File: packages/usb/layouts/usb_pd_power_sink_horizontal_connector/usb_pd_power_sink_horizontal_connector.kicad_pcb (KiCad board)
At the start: 2 copper layers, 8 parts, among them U2 2.9V

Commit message: WIP update usb
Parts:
- C1: value 1µF ±10% 16V X5R -> 1µF ±10% 25V X5R; footprint atopile:C0402-b3ef17 -> Samsung_Electro_Mechanics_CL05A105KA5NQNC:C0402
- R1, R2, R4: footprint atopile:R0402-56259e -> UNI_ROYAL_0402WGF1002TCE:R0402
- R3: footprint atopile:R0402-56259e -> UNI_ROYAL_0402WGF1001TCE:R0402
- U1: footprint atopile:ESSOP-10_L4.9-W3.9-P1.0-LS6.0-TL-EP-20a8ca -> WCH_CH224K:ESSOP-10_L4.9-W3.9-P1.0-LS6.0-TL-EP
- U2: footprint lib:LED0603-RD -> Hubei_KENTO_Elec_Blue_light_0603:LED0603-RD
- X1: footprint atopile:USB-C-SMD_TYPE-C-6PIN-2MD-073-1d78f0 -> SHOU_HAN_TYPE_C_16PIN_2MD_073:USB-C-SMD_TYPE-C-6PIN-2MD-073
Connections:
- U1 pad 2: pd_trigger.controller-line -> pd_trigger.controller-line-1
- U1 pad 3: pd_trigger.controller-line-1 -> pd_trigger.controller-line
- U1 pad 4: line-1 -> line-4
- U1 pad 6: line -> line-5
- X1 pad : (no net) -> net
- X1 pad 10: line -> line-5
- X1 pad 3: line-4 -> line
- X1 pad 6: line-1 -> line-4
- X1 pad 8: line-1 -> line-4
- X1 pad 9: line-5 -> line-1
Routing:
- net line-5: track 0.00 -> 13.6 mm, vias 0 -> 2
- net line: track 13.6 -> 0.00 mm, vias 2 -> 0
- net line-4: track 0.00 -> 8.15 mm, vias 0 -> 2
- net line-1: track 8.15 -> 0.00 mm, vias 2 -> 0

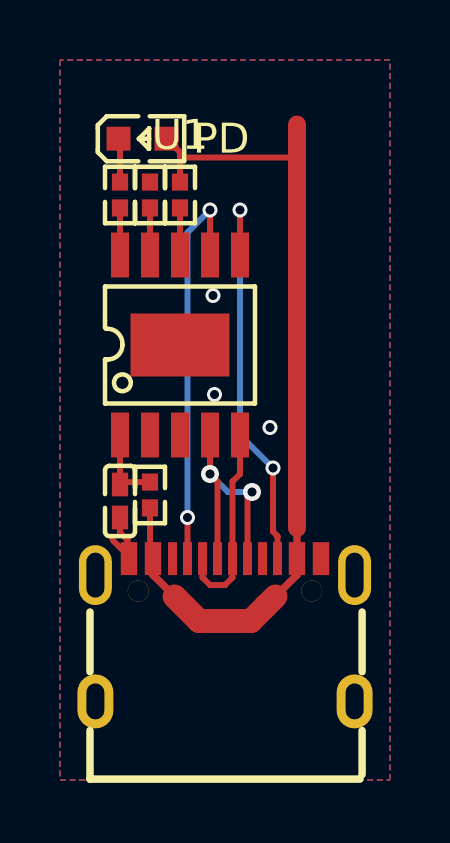
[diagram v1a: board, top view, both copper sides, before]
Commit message: Manually fix fp lib tables
fix some small bugs
fix package only modules (e.g. logos)
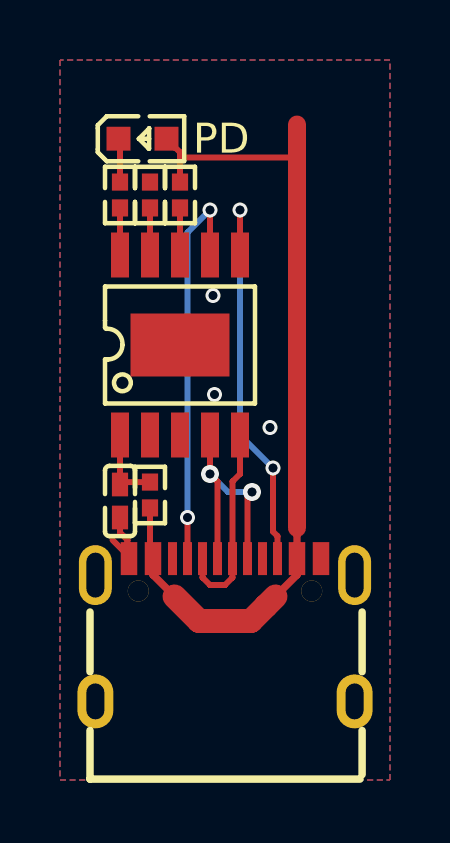
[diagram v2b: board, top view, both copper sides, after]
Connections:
- U1 pad 2: pd_trigger.controller-line-1 -> pd_trigger.controller-line
- U1 pad 3: pd_trigger.controller-line -> pd_trigger.controller-line-1
- U1 pad 4: line-4 -> line-1
- U1 pad 5: line-2 -> line-4
- U1 pad 6: line-5 -> line-2
- U1 pad 7: line-3 -> line
- X1 pad 10: line-5 -> line-2
- X1 pad 3: line -> line-3
- X1 pad 4: line-3 -> line
- X1 pad 5: line-2 -> line-4
- X1 pad 6: line-4 -> line-1
- X1 pad 7: line-2 -> line-4
- X1 pad 8: line-4 -> line-1
- X1 pad 9: line-1 -> line-5
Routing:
- net line-5: track 13.6 -> 0.00 mm, vias 2 -> 0
- net line-3: track 13.4 -> 0.00 mm, vias 2 -> 0
- net line: track 0.00 -> 13.4 mm, vias 0 -> 2
- net line-1: track 0.00 -> 8.15 mm, vias 0 -> 2
- net line-2: track 6.69 -> 13.6 mm, vias 0 -> 2
- net line-4: track 8.15 -> 6.69 mm, vias 2 -> 0

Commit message: rebuild all packages & regenerate images of changed layouts (silk)
Add new scripts for version bump and build (based on atopile/packages)
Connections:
- R2 pad 2: pd_trigger-line -> pd_trigger-line-1
- R4 pad 1: pd_trigger-line-1 -> pd_trigger-line
- U1 pad 4: line-1 -> line-5
- U1 pad 6: line-2 -> line-1
- U1 pad 8: pd_trigger-line -> pd_trigger-line-1
- U1 pad 9: pd_trigger-line-1 -> pd_trigger-line
- X1 pad 10: line-2 -> line-1
- X1 pad 6: line-1 -> line-5
- X1 pad 8: line-1 -> line-5
- X1 pad 9: line-5 -> line-2
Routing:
- net line-2: track 13.6 -> 0.00 mm, vias 2 -> 0
- net line-5: track 0.00 -> 8.15 mm, vias 0 -> 2
- net line-1: track 8.15 -> 13.6 mm
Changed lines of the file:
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@@
     (net 1 "pd_trigger.controller-line-1")
     (net 2 "pd_trigger.controller-line")
-    (net 3 "pd_trigger-line")
+    (net 3 "pd_trigger-line-1")
     (net 4 "hv")
-    (net 5 "pd_trigger-line-1")
+    (net 5 "pd_trigger-line")
     (net 6 "pd_trigger-gnd")
     (net 7 "cathode")
-    (net 8 "line-2")
+    (net 8 "line-1")
     (net 9 "line-3")
     (net 10 "anode")
-    (net 11 "line-5")
+    (net 11 "line-2")
     (net 12 "gnd")
     (net 13 "line-4")
-    (net 14 "line-1")
+    (net 14 "line-5")
     (net 15 "line")
     (net 16 "net")
@@
             (size 0.57 0.54)
             (layers "F.Cu" "F.Paste" "F.Mask")
-            (net 5 "pd_trigger-line-1")
+            (net 5 "pd_trigger-line")
         )
         (model "${KIPRJMOD}/../../parts/UNI_ROYAL_0402WGF1002TCE/R0402_L1.0-W0.5-H0.4.step"
@@
             )
         )
-        (property "__atopile_lib_fp_hash__" "67c8cb14-7a56-5f37-cd49-de206344da21"
+        (property "__atopile_lib_fp_hash__" "316ee354-f06d-0bd8-88cd-489840625970"
             (at 0 0 0)
             (layer "User.9")
@@
             )
         )
-        (property "checksum" "92e079f9d1334f588ddb127873738a56bad1b8f57794e6d8826a1dbb9b5fecef"
+        (property "checksum" "84749ec1cd5fbb3976a4ef85d04dc245f71ce15cbd4539127e07cf8da310f7ce"
             (at 0 0 0)
             (layer "User.9")
@@
             (size 1.5 0.6)
             (layers "F.Cu" "F.Mask" "F.Paste")
-            (net 14 "line-1")
+            (net 14 "line-5")
         )
         (pad "5" smd rect
@@
             (size 1.5 0.6)
             (layers "F.Cu" "F.Mask" "F.Paste")
-            (net 8 "line-2")
+            (net 8 "line-1")
         )
         (pad "7" smd rect
@@
             (size 1.5 0.6)
             (layers "F.Cu" "F.Mask" "F.Paste")
-            (net 3 "pd_trigger-line")
+            (net 3 "pd_trigger-line-1")
         )
         (pad "9" smd rect
@@
             (size 1.5 0.6)
             (layers "F.Cu" "F.Mask" "F.Paste")
-            (net 5 "pd_trigger-line-1")
+            (net 5 "pd_trigger-line")
         )
         (pad "10" smd rect
@@
             (size 0.3 1.1)
             (layers "F.Cu" "F.Mask" "F.Paste")
-            (net 14 "line-1")
+            (net 14 "line-5")
         )
         (pad "7" smd rect
@@
             (size 0.3 1.1)
             (layers "F.Cu" "F.Mask" "F.Paste")
-            (net 14 "line-1")
+            (net 14 "line-5")
         )
         (pad "9" smd rect
@@
             (size 0.3 1.1)
             (layers "F.Cu" "F.Mask" "F.Paste")
-            (net 11 "line-5")
+            (net 11 "line-2")
         )
         (pad "10" smd rect
@@
             (size 0.3 1.1)
             (layers "F.Cu" "F.Mask" "F.Paste")
-            (net 8 "line-2")
+            (net 8 "line-1")
         )
         (pad "11" smd rect
@@
             (size 0.57 0.54)
             (layers "F.Cu" "F.Paste" "F.Mask")
-            (net 3 "pd_trigger-line")
+            (net 3 "pd_trigger-line-1")
         )
         (pad "1" smd rect

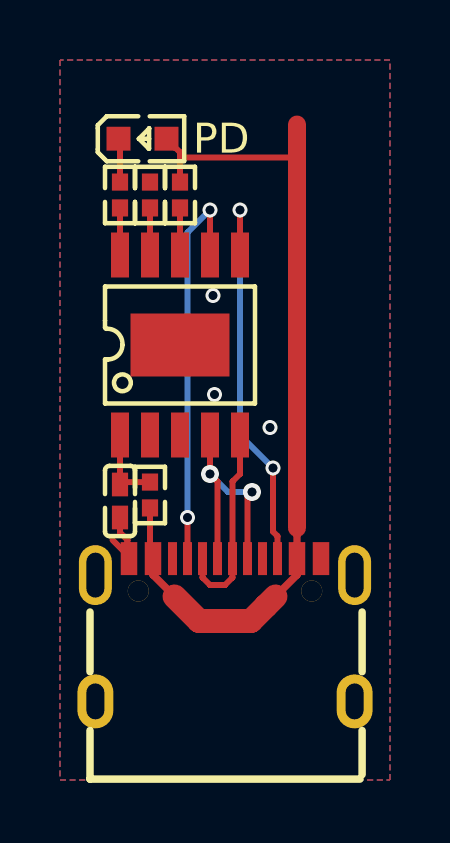
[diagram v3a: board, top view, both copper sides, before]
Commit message: Use packages from packages folder
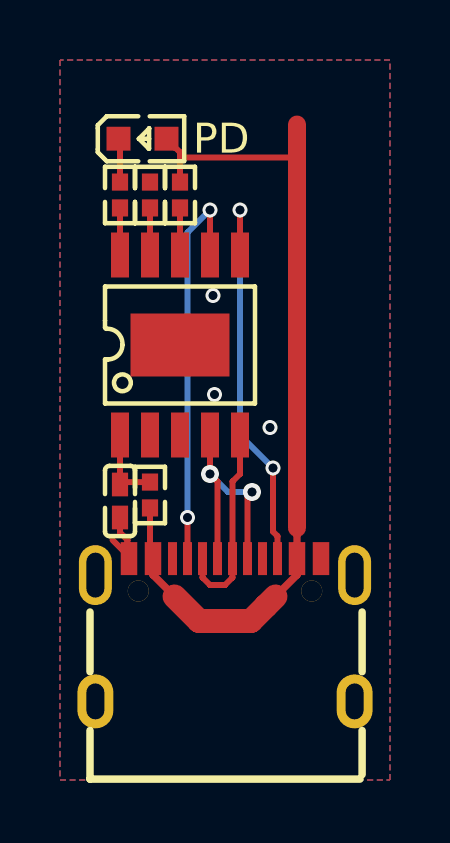
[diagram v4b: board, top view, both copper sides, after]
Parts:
- removed U2: 2.9V, Hubei_KENTO_Elec_Blue_light_0603:LED0603-RD
- added LED1: , Hubei_KENTO_Elec_Blue_light_0603:LED0603-RD, F.Cu at (-2.75, -16.4)
